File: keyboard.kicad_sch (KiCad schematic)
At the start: 27 parts, among them J1 USB_C_Receptacle_USB2.0_14P, SW1 SW_Push, SW2 SW_Push, SW3 SW_Push, SW4 SW_Push, SW5 SW_Push, U1 ATmega32U4-A, Y1 Crystal_GND24_Small

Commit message: bad
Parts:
- removed J1: USB_C_Receptacle_USB2.0_14P, symbol Connector:USB_C_Receptacle_USB2.0_14P
- removed SW1: SW_Push, symbol Switch:SW_Push
- added J1: USB4085-GF-A_REVB, USB-C:GCT_USB4085-GF-A_REVB, symbol USB4085-GF-A_REVB:USB4085-GF-A_REVB
- added S1: 8-1437565-1, Button:SW_8-1437565-1, symbol 8-1437565-1:8-1437565-1
- SW2, SW3, SW4, SW5: footprint (none) -> MX_keys:MX-Hotswap-1U
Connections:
- net +5V: no longer C1.2, C7.2, C8.2, R1.2, R5.2, R6.2, U1.15 (GND), U1.23 (GND), U1.35 (GND), U1.43 (GND), U1.5 (UGND), Y1.2, Y1.4
- net D+: now also J1.A6 (DP1), J1.B6 (DP2)
- net D-: now also J1.A7 (DN1), J1.B7 (DN2)
- net VCC: now also J1.A4 (VBUS), J1.A9 (VBUS), J1.B4 (VBUS), J1.B9 (VBUS)
- net X0: now also U1.8 (PB0)
- net X1: now also U1.9 (PB1)
- net Y0: now also U1.10 (PB2)
- net Y1: now also U1.11 (PB3)
- net at R4.2, U1.13 (~{RESET}): now also S1.3, S1.4
- net GND: now reaches C2.1, C3.1, C4.1, C5.1, C6.1
- net GND: now also C1.2, C7.2, C8.2, R1.2, R5.2, R6.2, U1.15 (GND), U1.23 (GND), U1.35 (GND), U1.43 (GND), U1.5 (UGND), Y1.2, Y1.4, J1.A1 (GND), J1.A12 (GND), J1.B1 (GND), J1.B12 (GND), S1.1, S1.2
- net at R6.1: now also J1.B5 (CC2)
- net at R5.1: now also J1.A5 (CC1)
- new net: J1.S1 (SHELL), J1.S2 (SHELL), J1.S3 (SHELL), J1.S4 (SHELL)

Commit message: V1
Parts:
- removed F1: 500mA, Fuse:Fuse_1206_3216Metric, symbol Device:Polyfuse
- removed J1: USB4085-GF-A_REVB, USB-C:GCT_USB4085-GF-A_REVB, symbol USB4085-GF-A_REVB:USB4085-GF-A_REVB
- removed R5, R6: 5.1k, Resistor_SMD:R_0805_2012Metric, symbol Device:R_Small_US
- removed S1: 8-1437565-1, Button:SW_8-1437565-1, symbol 8-1437565-1:8-1437565-1
- added 5V+2, GND1: Power, TestPoint:TestPoint_Pad_1.0x1.0mm, symbol Connector:TestPoint
- added Custom-1, Custom-2, Custom-3, Custom-4, Custom-5, Key_*1, Key_-1, Key_1, Key_2, Key_3, Key_4, Key_5, Key_6, Key_9, Key_del1: SW_Push, MX_keys:MX-Hotswap-1U, symbol Switch:SW_Push
- added D+1: D+, TestPoint:TestPoint_Pad_1.0x1.0mm, symbol Connector:TestPoint
- added D-1: D-, TestPoint:TestPoint_Pad_1.0x1.0mm, symbol Connector:TestPoint
- added D10, D11, D12, D13, D14, D16, D17, D18, D19, D20, D21, D23, D25, D5, D6, D7, D8, D9: D_Small, Diode_SMD:D_SOD-123, symbol Device:D_Small
- added F2: 500mA, Fuse:Fuse_1206_3216Metric, symbol Device:Polyfuse
- added J2: TYPE-C-31-M-12, USB-C:HRO_TYPE-C-31-M-12, symbol MyLib:TYPE-C-31-M-12
- added Key_+1, Key_enter1: SW_Push_U2, Button_Switch_Keyboard:MX-Hotswap-2U-Vertical-ReversedStabilizers, symbol Switch:SW_Push
- added Key_0: SW_Push_U2, Button_Switch_Keyboard:MX-Hotswap-2U-ReversedStabilizers, symbol Switch:SW_Push
- added R7, R8: 5.1k, Resistor_SMD:R_0805_2012Metric, symbol Device:R_Small_US
- added S2: TS-1187A-B-A-B, USB-C:SW_TS-1187A-B-A-B, symbol MyLib:TS-1187A-B-A-B
- added TV1: ~, Button_Switch_Keyboard:SOT-23-6_L2.9-W1.6-P0.95-LS2.8-BR, symbol MyLib:SRV05-4-P-T7
- C1: LCSC (none) -> C28323
- C2, C3, C4: LCSC (none) -> C49678
- C5: LSCS (none) -> C49678
- C6: LCSC (none) -> C15850
- C7: LCSC (none) -> C1804
- C8: LSCS (none) -> C1804
- D1, D2: LCSC (none) -> C64898
- NumLock1: renamed from SW2; LCSC (none) -> C41430893
- R1, R4: LCSC (none) -> C17414
- R2, R3: LCSC (none) -> C17561
- Y1: LCSC (none) -> C13738
- renumbered SW3 to Key_/1, SW4 to Key_7, SW5 to Key_8
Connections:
- net +5V: now also 5V+2.1, F2.2
- net D+: now also D+1.1, J2.A6 (DP1), J2.B6 (DP2), TV1.6
- net D-: now also D-1.1, J2.A7 (DN1), J2.B7 (DN2), TV1.1
- net GND: now also GND1.1, J2.A1_B12 (GND), J2.B1_A12 (GND), J2.S1 (SHIELD), J2.S2 (SHIELD), J2.S3 (SHIELD), J2.S4 (SHIELD), R7.1, R8.1, S2.A, S2.B, TV1.2
- net VCC: now also F2.1, J2.A4_B9 (VBUS), J2.B4_A9 (VBUS), TV1.5
- net X0: now also U1.36 (PF7), D11.1 (K), D17.1 (K), D9.1 (K); no longer U1.8 (PB0)
- net X1: now also U1.37 (PF6), D10.1 (K), D12.1 (K), D18.1 (K); no longer U1.9 (PB1)
- net Y0: now also U1.29 (PB5), Key_0.2, Key_1.2, Key_4.2; no longer U1.10 (PB2)
- net Y1: now also U1.28 (PB4), Key_2.2, Key_5.2; no longer U1.11 (PB3)
- net at R4.2, U1.13 (~{RESET}): now also S2.C, S2.D
- net Y3: now reaches U1.26 (PD6)
- net Y3: now also Key_+1.2, Key_-1.2, Key_enter1.2
- net Y2: now reaches U1.27 (PD7)
- net Y2: now also Key_*1.2, Key_3.2, Key_6.2, Key_9.2, Key_del1.2
- net X4: now reaches U1.38 (PF5)
- net X4: now also D21.1 (K), D23.1 (K), D25.1 (K)
- net X3: now reaches U1.39 (PF4)
- net X3: now also D14.1 (K), D16.1 (K), D20.1 (K), D6.1 (K), D8.1 (K)
- net X2: now reaches U1.40 (PF1)
- net X2: now also D13.1 (K), D19.1 (K), D5.1 (K), D7.1 (K)
- new net: D12.2 (A), Key_+1.1
- new net: D14.2 (A), Key_3.1
- new net: D11.2 (A), Key_-1.1
- new net: Custom-3.1, D19.2 (A)
- new net: D21.2 (A), Key_0.1
- new net: D16.2 (A), Key_enter1.1
- new net: D10.2 (A), Key_9.1
- new net: Custom-5.1, D25.2 (A)
- new net: D7.2 (A), Key_5.1
- new net: D6.2 (A), Key_1.1
- new net: D23.2 (A), Key_del1.1
- new net: D8.2 (A), Key_2.1
- new net: Custom-4.1, D20.2 (A)
- new net: Custom-2.1, D18.2 (A)
- new net: Custom-1.1, D17.2 (A)
- new net: D9.2 (A), Key_*1.1
- new net: D5.2 (A), Key_4.1
- new net: D13.2 (A), Key_6.1
- new net CC1: J2.A5 (CC1), R8.2, TV1.3
- new net CC2: J2.B5 (CC2), R7.2, TV1.4
- new net Y4: Custom-1.2, Custom-2.2, Custom-3.2, Custom-4.2, Custom-5.2, U1.9 (PB1)
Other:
- note added: "By: skellieton"

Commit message: fixFlip
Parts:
- Key_+1, Key_enter1: footprint Button_Switch_Keyboard:MX-Hotswap-2U-Vertical-ReversedStabilizers -> Button_Switch_Keyboard:MX-Hotswap-2U-ReversedStabilizers
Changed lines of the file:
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@@
 			)
 		)
-		(property "Footprint" "Button_Switch_Keyboard:MX-Hotswap-2U-Vertical-ReversedStabilizers"
+		(property "Footprint" "Button_Switch_Keyboard:MX-Hotswap-2U-ReversedStabilizers"
 			(at 246.38 88.9 0)
 			(effects
@@
 			)
 		)
-		(property "Footprint" "Button_Switch_Keyboard:MX-Hotswap-2U-Vertical-ReversedStabilizers"
+		(property "Footprint" "Button_Switch_Keyboard:MX-Hotswap-2U-ReversedStabilizers"
 			(at 246.38 120.65 0)
 			(effects

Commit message: V1-with-led-schem
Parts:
- added C10, C11, C12, C13, C14, C15, C16, C17, C18, C19, C20, C21, C22, C23, C24, C25, C27, C28, C29, C30, C31, C9: C_Small, Capacitor_SMD:C_0805_2012Metric, symbol Device:C_Small
- added U10, U11, U16, U17, U18, U20, U21, U7, U8, U9: ~, MyLiB:MX-SK-E-Right_Left, symbol MyLib:SK6812MINI-E_C5149201
- added U12, U13, U14, U15, U2, U22, U23, U24, U3, U4, U5, U6: ~, MyLiB:MX-SK-E-Left_Right, symbol MyLib:SK6812MINI-E_C5149201
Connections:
- net +5V: now also C10.2, C11.2, C12.2, C13.2, C14.2, C15.2, C16.2, C17.2, C18.2, C19.2, C20.2, C21.2, C22.2, C23.2, C24.2, C25.2, C27.2, C28.2, C29.2, C30.2, C31.2, C9.2, U10.1 (VDD), U11.1 (VDD), U12.1 (VDD), U13.1 (VDD), U14.1 (VDD), U15.1 (VDD), U16.1 (VDD), U17.1 (VDD), U18.1 (VDD), U2.1 (VDD), U20.1 (VDD), U21.1 (VDD), U22.1 (VDD), U23.1 (VDD), U24.1 (VDD), U3.1 (VDD), U4.1 (VDD), U5.1 (VDD), U6.1 (VDD), U7.1 (VDD), U8.1 (VDD), U9.1 (VDD)
- net GND: now also C10.1, C11.1, C12.1, C13.1, C14.1, C15.1, C16.1, C17.1, C18.1, C19.1, C20.1, C21.1, C22.1, C23.1, C24.1, C25.1, C27.1, C28.1, C29.1, C30.1, C31.1, C9.1, U10.3 (GND), U11.3 (GND), U12.3 (GND), U13.3 (GND), U14.3 (GND), U15.3 (GND), U16.3 (GND), U17.3 (GND), U18.3 (GND), U2.3 (GND), U20.3 (GND), U21.3 (GND), U22.3 (GND), U23.3 (GND), U24.3 (GND), U3.3 (GND), U4.3 (GND), U5.3 (GND), U6.3 (GND), U7.3 (GND), U8.3 (GND), U9.3 (GND)
- new net: U12.2 (DOUT), U13.4 (DIN)
- new net: U11.2 (DOUT), U12.4 (DIN)
- new net: U22.2 (DOUT), U23.4 (DIN)
- new net: U21.2 (DOUT), U22.4 (DIN)
- new net: U20.2 (DOUT), U21.4 (DIN)
- new net: U15.2 (DOUT), U16.4 (DIN)
- new net: U14.2 (DOUT), U15.4 (DIN)
- new net: U16.2 (DOUT), U17.4 (DIN)
- new net: U3.2 (DOUT), U4.4 (DIN)
- new net: U2.2 (DOUT), U3.4 (DIN)
- new net: U7.2 (DOUT), U8.4 (DIN)
- new net: U6.2 (DOUT), U7.4 (DIN)
- new net: U17.2 (DOUT), U18.4 (DIN)
- new net: U10.4 (DIN), U9.2 (DOUT)
- new net: U8.2 (DOUT), U9.4 (DIN)
- new net: U23.2 (DOUT), U24.4 (DIN)
- new net: U13.2 (DOUT), U14.4 (DIN)
- new net: U5.2 (DOUT), U6.4 (DIN)
- new net: U4.2 (DOUT), U5.4 (DIN)
- new net LED_DATA_1: U10.2 (DOUT)
- new net LED_DATA_2: U18.2 (DOUT), U20.4 (DIN)
- new net LED_DATA_IN: U2.4 (DIN)
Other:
- moved on the sheet: C2, C3, C4, C5, C6, Custom-1, Custom-2, Custom-3, Custom-4, Custom-5, Key_*1, Key_+1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

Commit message: V2-led
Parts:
- added C26: 10uf, Capacitor_SMD:C_0805_2012Metric, symbol Device:C_Small
- added R5: 500, Resistor_SMD:R_0805_2012Metric, symbol Device:R_Small_US
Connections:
- net +5V: now also C26.2
- net GND: now also C26.1
- net LED_DATA_1: now also U11.4 (DIN)
- net LED_DATA_IN: now also R5.2
- net at U1.41 (PF0): now also R5.1
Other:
- moved on the sheet: C5

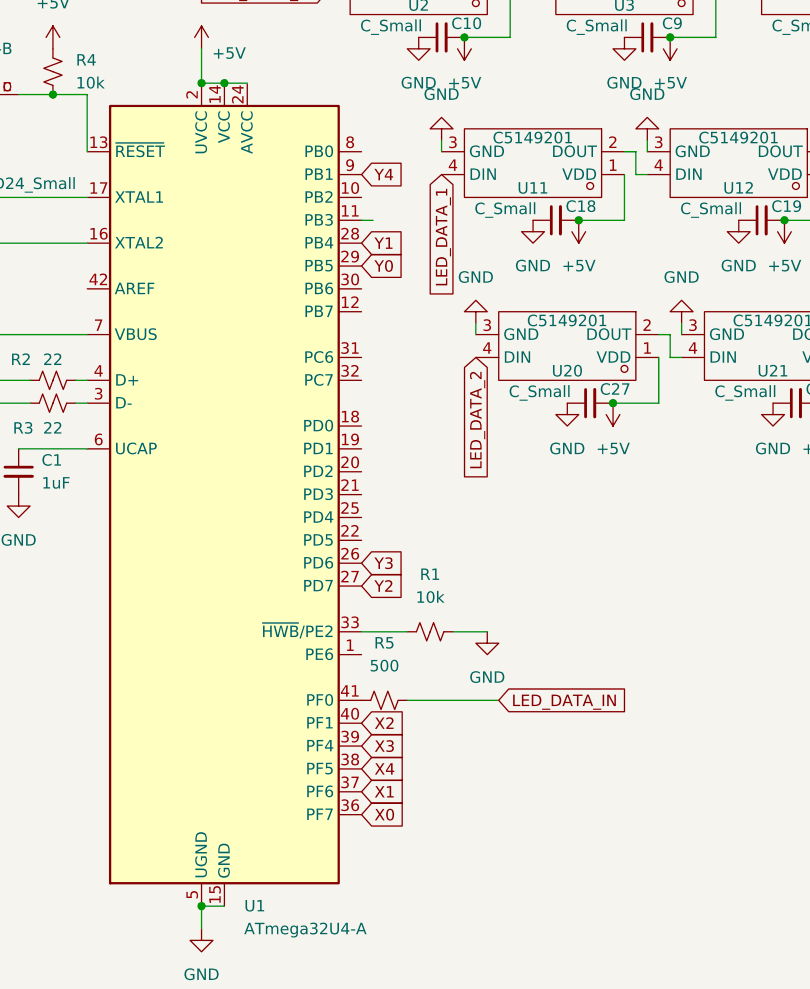
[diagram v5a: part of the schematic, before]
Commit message: V2.1, used a grounding plane
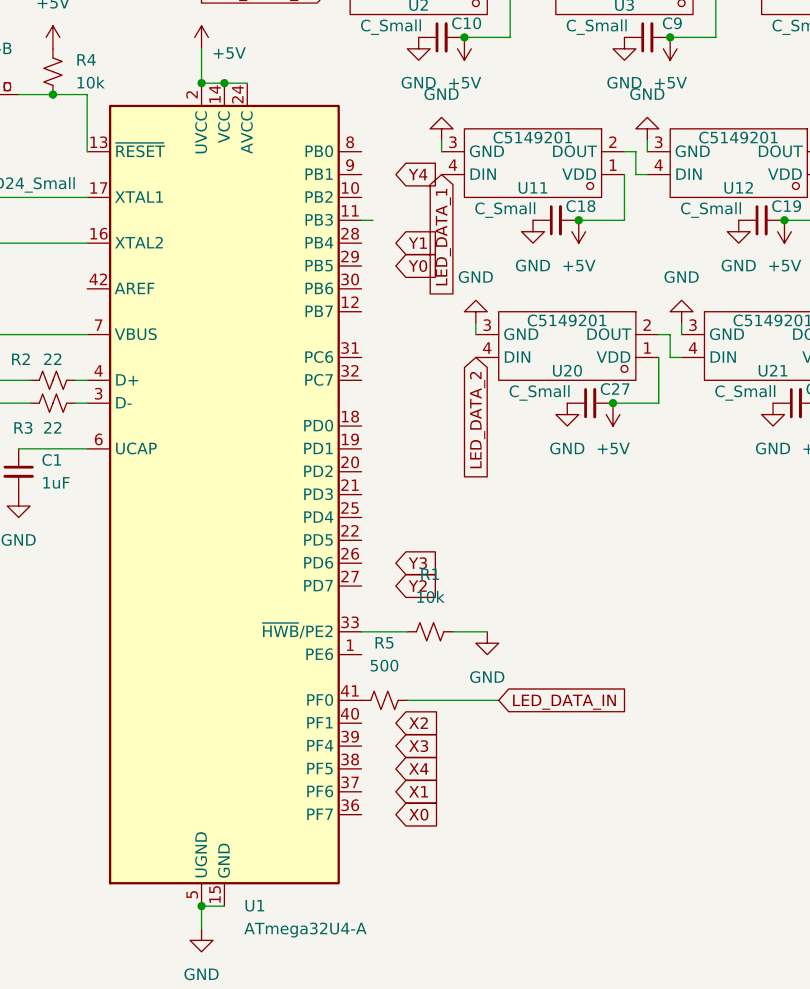
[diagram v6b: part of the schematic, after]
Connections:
- net X0: no longer U1.36 (PF7)
- net X1: no longer U1.37 (PF6)
- net X2: no longer U1.40 (PF1)
- net X3: no longer U1.39 (PF4)
- net X4: no longer U1.38 (PF5)
- net Y0: no longer U1.29 (PB5)
- net Y1: no longer U1.28 (PB4)
- net Y2: no longer U1.27 (PD7)
- net Y3: no longer U1.26 (PD6)
- net Y4: no longer U1.9 (PB1)

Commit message: upaded islands
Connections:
- net X0: now also U1.36 (PF7)
- net X1: now also U1.37 (PF6)
- net X2: now also U1.40 (PF1)
- net X3: now also U1.39 (PF4)
- net X4: now also U1.38 (PF5)
- net Y0: now also U1.29 (PB5)
- net Y1: now also U1.28 (PB4)
- net Y2: now also U1.27 (PD7)
- net Y3: now also U1.26 (PD6)
- net Y4: now also U1.9 (PB1)
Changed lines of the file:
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@@
 	(global_label "Y2"
 		(shape input)
-		(at 82.55 86.36 0)
-		(fields_autoplaced yes)
-		(effects
-			(font
-				(size 1.27 1.27)
-			)
-			(justify left)
-		)
-		(property "Intersheetrefs" "${INTERSHEET_REFS}"
-			(at 87.8333 86.36 0)
+		(at 78.74 86.36 0)
+		(fields_autoplaced yes)
+		(effects
+			(font
+				(size 1.27 1.27)
+			)
+			(justify left)
+		)
+		(property "Intersheetrefs" "${INTERSHEET_REFS}"
+			(at 84.0233 86.36 0)
 			(effects
 				(font
@@
 	(global_label "Y1"
 		(shape input)
-		(at 82.55 48.26 0)
-		(fields_autoplaced yes)
-		(effects
-			(font
-				(size 1.27 1.27)
-			)
-			(justify left)
-		)
-		(property "Intersheetrefs" "${INTERSHEET_REFS}"
-			(at 87.8333 48.26 0)
+		(at 78.74 48.26 0)
+		(fields_autoplaced yes)
+		(effects
+			(font
+				(size 1.27 1.27)
+			)
+			(justify left)
+		)
+		(property "Intersheetrefs" "${INTERSHEET_REFS}"
+			(at 84.0233 48.26 0)
 			(effects
 				(font
@@
 	(global_label "Y3"
 		(shape input)
-		(at 82.55 83.82 0)
-		(fields_autoplaced yes)
-		(effects
-			(font
-				(size 1.27 1.27)
-			)
-			(justify left)
-		)
-		(property "Intersheetrefs" "${INTERSHEET_REFS}"
-			(at 87.8333 83.82 0)
+		(at 78.74 83.82 0)
+		(fields_autoplaced yes)
+		(effects
+			(font
+				(size 1.27 1.27)
+			)
+			(justify left)
+		)
+		(property "Intersheetrefs" "${INTERSHEET_REFS}"
+			(at 84.0233 83.82 0)
 			(effects
 				(font
@@
 	(global_label "X0"
 		(shape input)
-		(at 82.55 111.76 0)
-		(fields_autoplaced yes)
-		(effects
-			(font
-				(size 1.27 1.27)
-			)
-			(justify left)
-		)
-		(property "Intersheetrefs" "${INTERSHEET_REFS}"
-			(at 87.9542 111.76 0)
+		(at 78.74 111.76 0)
+		(fields_autoplaced yes)
+		(effects
+			(font
+				(size 1.27 1.27)
+			)
+			(justify left)
+		)
+		(property "Intersheetrefs" "${INTERSHEET_REFS}"
+			(at 84.1442 111.76 0)
 			(effects
 				(font
@@
 	(global_label "X2"
 		(shape input)
-		(at 82.55 101.6 0)
-		(fields_autoplaced yes)
-		(effects
-			(font
-				(size 1.27 1.27)
-			)
-			(justify left)
-		)
-		(property "Intersheetrefs" "${INTERSHEET_REFS}"
-			(at 87.9542 101.6 0)
+		(at 78.74 101.6 0)
+		(fields_autoplaced yes)
+		(effects
+			(font
+				(size 1.27 1.27)
+			)
+			(justify left)
+		)
+		(property "Intersheetrefs" "${INTERSHEET_REFS}"
+			(at 84.1442 101.6 0)
 			(effects
 				(font
@@
 	(global_label "Y0"
 		(shape input)
-		(at 82.55 50.8 0)
-		(fields_autoplaced yes)
-		(effects
-			(font
-				(size 1.27 1.27)
-			)
-			(justify left)
-		)
-		(property "Intersheetrefs" "${INTERSHEET_REFS}"
-			(at 87.8333 50.8 0)
+		(at 78.74 50.8 0)
+		(fields_autoplaced yes)
+		(effects
+			(font
+				(size 1.27 1.27)
+			)
+			(justify left)
+		)
+		(property "Intersheetrefs" "${INTERSHEET_REFS}"
+			(at 84.0233 50.8 0)
 			(effects
 				(font
@@
 	(global_label "X1"
 		(shape input)
-		(at 82.55 109.22 0)
-		(fields_autoplaced yes)
-		(effects
-			(font
-				(size 1.27 1.27)
-			)
-			(justify left)
-		)
-		(property "Intersheetrefs" "${INTERSHEET_REFS}"
-			(at 87.9542 109.22 0)
+		(at 78.74 109.22 0)
+		(fields_autoplaced yes)
+		(effects
+			(font
+				(size 1.27 1.27)
+			)
+			(justify left)
+		)
+		(property "Intersheetrefs" "${INTERSHEET_REFS}"
+			(at 84.1442 109.22 0)
 			(effects
 				(font
@@
 	(global_label "X3"
 		(shape input)
-		(at 82.55 104.14 0)
-		(fields_autoplaced yes)
-		(effects
-			(font
-				(size 1.27 1.27)
-			)
-			(justify left)
-		)
-		(property "Intersheetrefs" "${INTERSHEET_REFS}"
-			(at 87.9542 104.14 0)
+		(at 78.74 104.14 0)
+		(fields_autoplaced yes)
+		(effects
+			(font
+				(size 1.27 1.27)
+			)
+			(justify left)
+		)
+		(property "Intersheetrefs" "${INTERSHEET_REFS}"
+			(at 84.1442 104.14 0)
 			(effects
 				(font
@@
 	(global_label "Y4"
 		(shape input)
-		(at 82.55 40.64 0)
-		(fields_autoplaced yes)
-		(effects
-			(font
-				(size 1.27 1.27)
-			)
-			(justify left)
-		)
-		(property "Intersheetrefs" "${INTERSHEET_REFS}"
-			(at 87.8333 40.64 0)
+		(at 78.74 40.64 0)
+		(fields_autoplaced yes)
+		(effects
+			(font
+				(size 1.27 1.27)
+			)
+			(justify left)
+		)
+		(property "Intersheetrefs" "${INTERSHEET_REFS}"
+			(at 84.0233 40.64 0)
 			(effects
 				(font
@@
 	(global_label "X4"
 		(shape input)
-		(at 82.55 106.68 0)
-		(fields_autoplaced yes)
-		(effects
-			(font
-				(size 1.27 1.27)
-			)
-			(justify left)
-		)
-		(property "Intersheetrefs" "${INTERSHEET_REFS}"
-			(at 87.9542 106.68 0)
-			(effects
-				(font
+		(at 78.74 106.68 0)
+		(fields_autoplaced yes)
+		(effects
+			(font
+				(size 1.27 1.27)
+			)
+			(justify left)
+		)
+		(property "Intersheetrefs" "${INTERSHEET_REFS}"
+			(at 84.1442 106.68 0)
+			(effects
+				(font

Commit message: added switch
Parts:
- added SW1: ~, MyLiB:SW-TH_MK-12D18-G040, symbol MyLib:MK-12D18-G020
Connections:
- net +5V: now also SW1.1, SW1.2
